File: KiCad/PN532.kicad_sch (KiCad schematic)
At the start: 56 parts, among them J1 Bell, J2 Header, J3 SPOX, SW1 TAMPER, U1 PN532, U2 QR, U3 QR, Y1 27.12MHz

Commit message: Gerenal KIcad 6 related tidy up
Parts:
- AJK1, AJK2: footprint RevK:AJK-Silk -> RevK:AJK
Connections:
- no-connect marks 15 -> 14

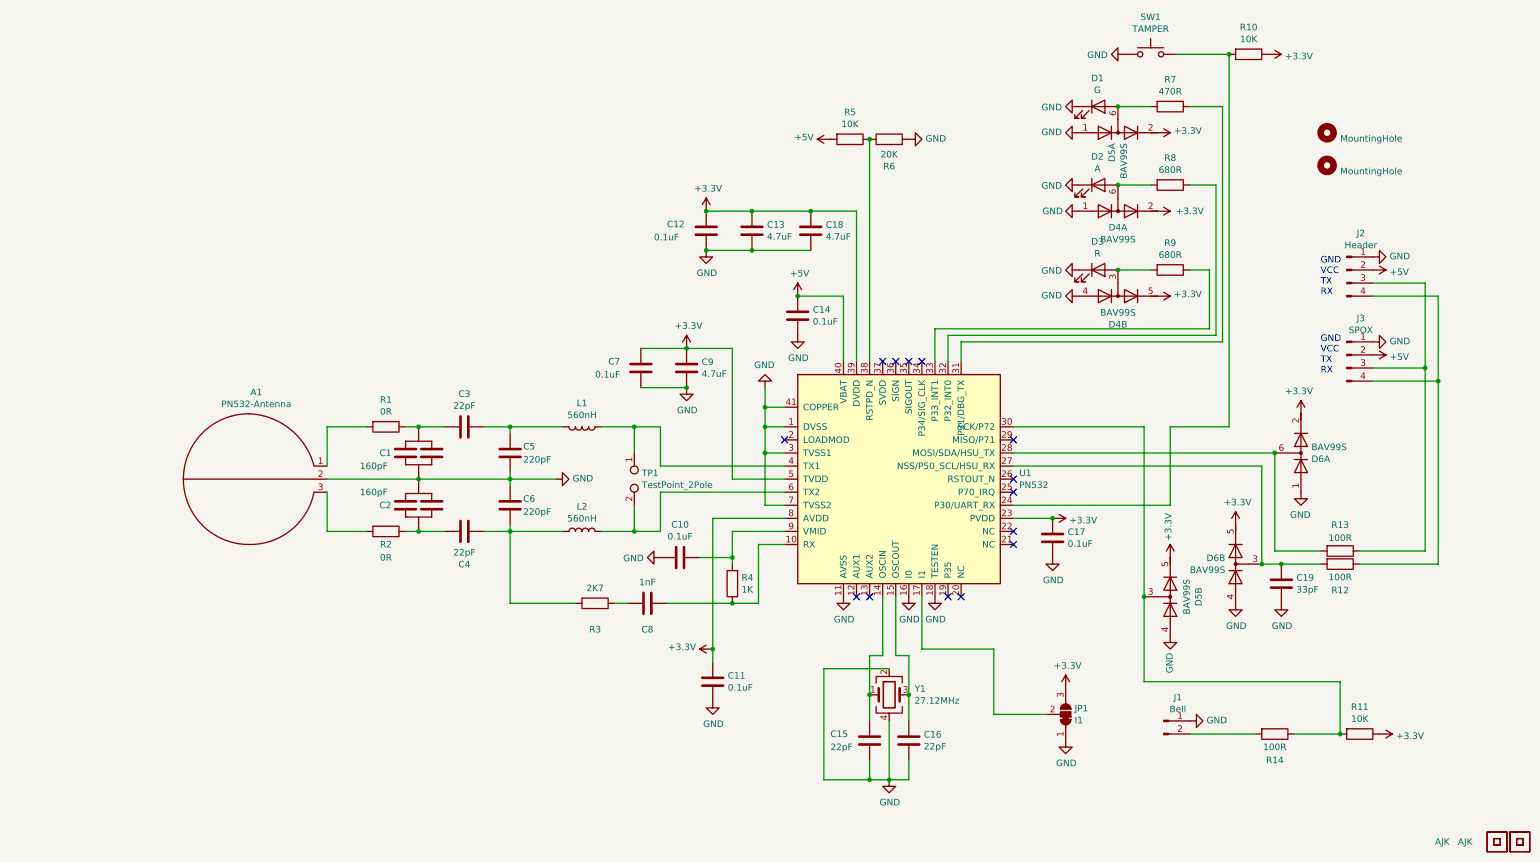
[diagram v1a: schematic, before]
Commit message: Reworked slightly to ensure 0R in BOM, and passing DRC cleanly under Kicad 6
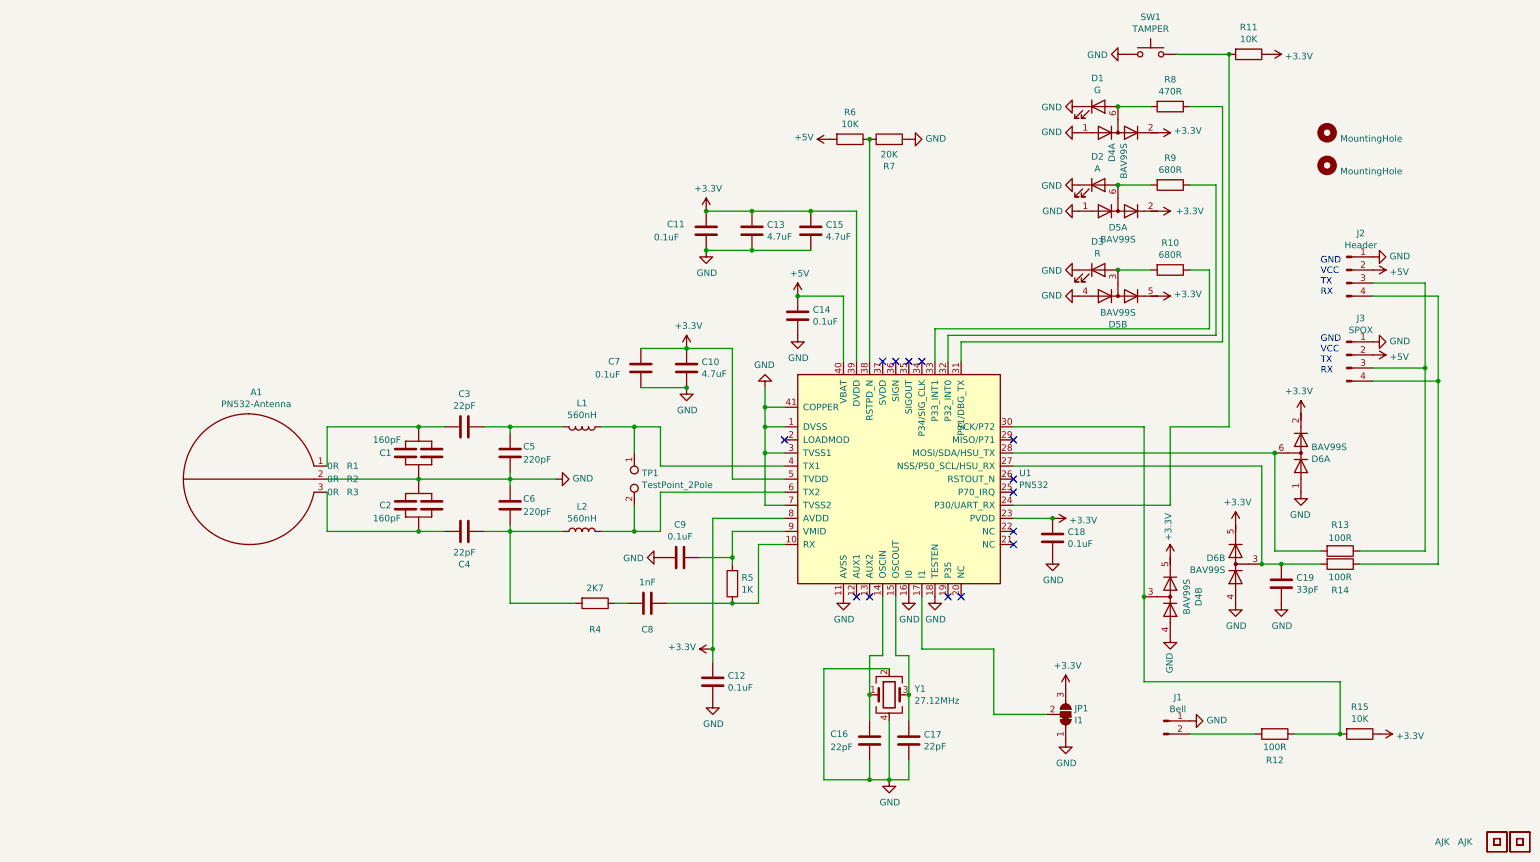
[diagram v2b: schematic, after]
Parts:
- removed R1, R2: 0R, RevK:R_0603, symbol Device:R
- added R1, R2, R3: 0R, RevK:Hidden, symbol RevK:Hidden
- renumbered AJK2 to AJK1, AJK1 to AJK2, C9 to C10, C12 to C11, C11 to C12, C18 to C15, C15 to C16, C16 to C17, C17 to C18, C10 to C9, D5 to D4, D4 to D5, R9 to R10, R10 to R11, R14 to R12, R12 to R14, R11 to R15, R3 to R4, R4 to R5, R5 to R6, R6 to R7, R7 to R8, R8 to R9, U3 to U2, U2 to U3
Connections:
- net at A1.1: now also C1.1, C3.2
- net at A1.3: now also C2.2, C4.1
